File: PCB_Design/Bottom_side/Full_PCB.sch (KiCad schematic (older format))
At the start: 0 parts

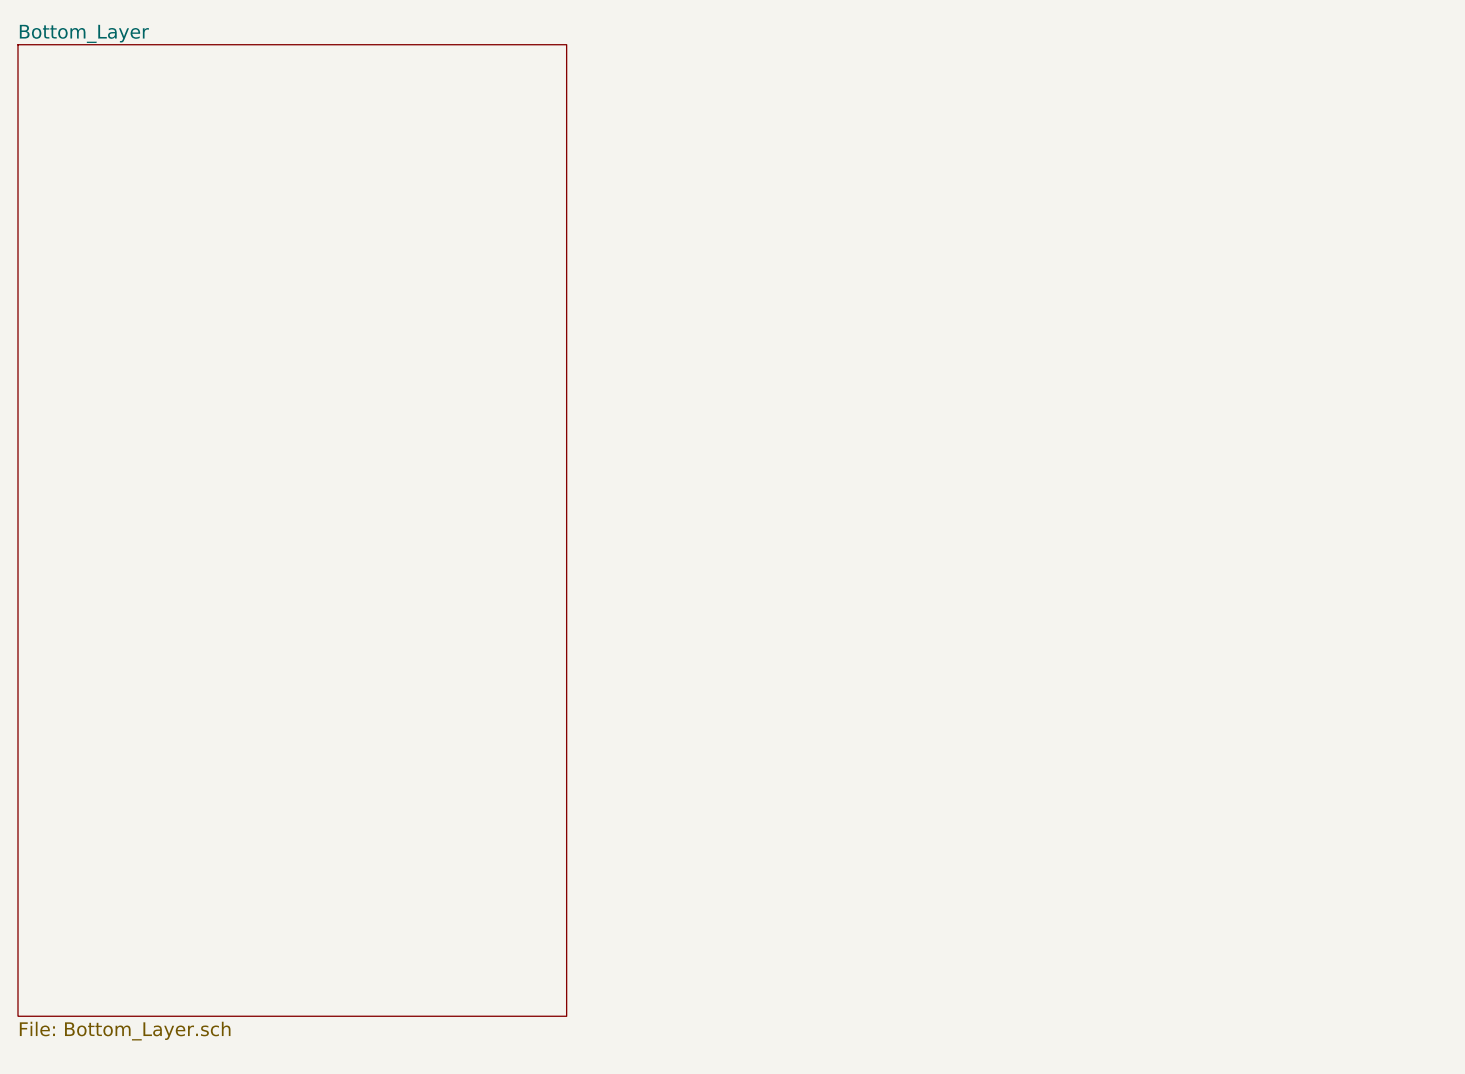
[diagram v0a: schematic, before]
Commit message: Updated PCB structure tree
Full_PCB now includes bottom and top layer hierarchical sheets
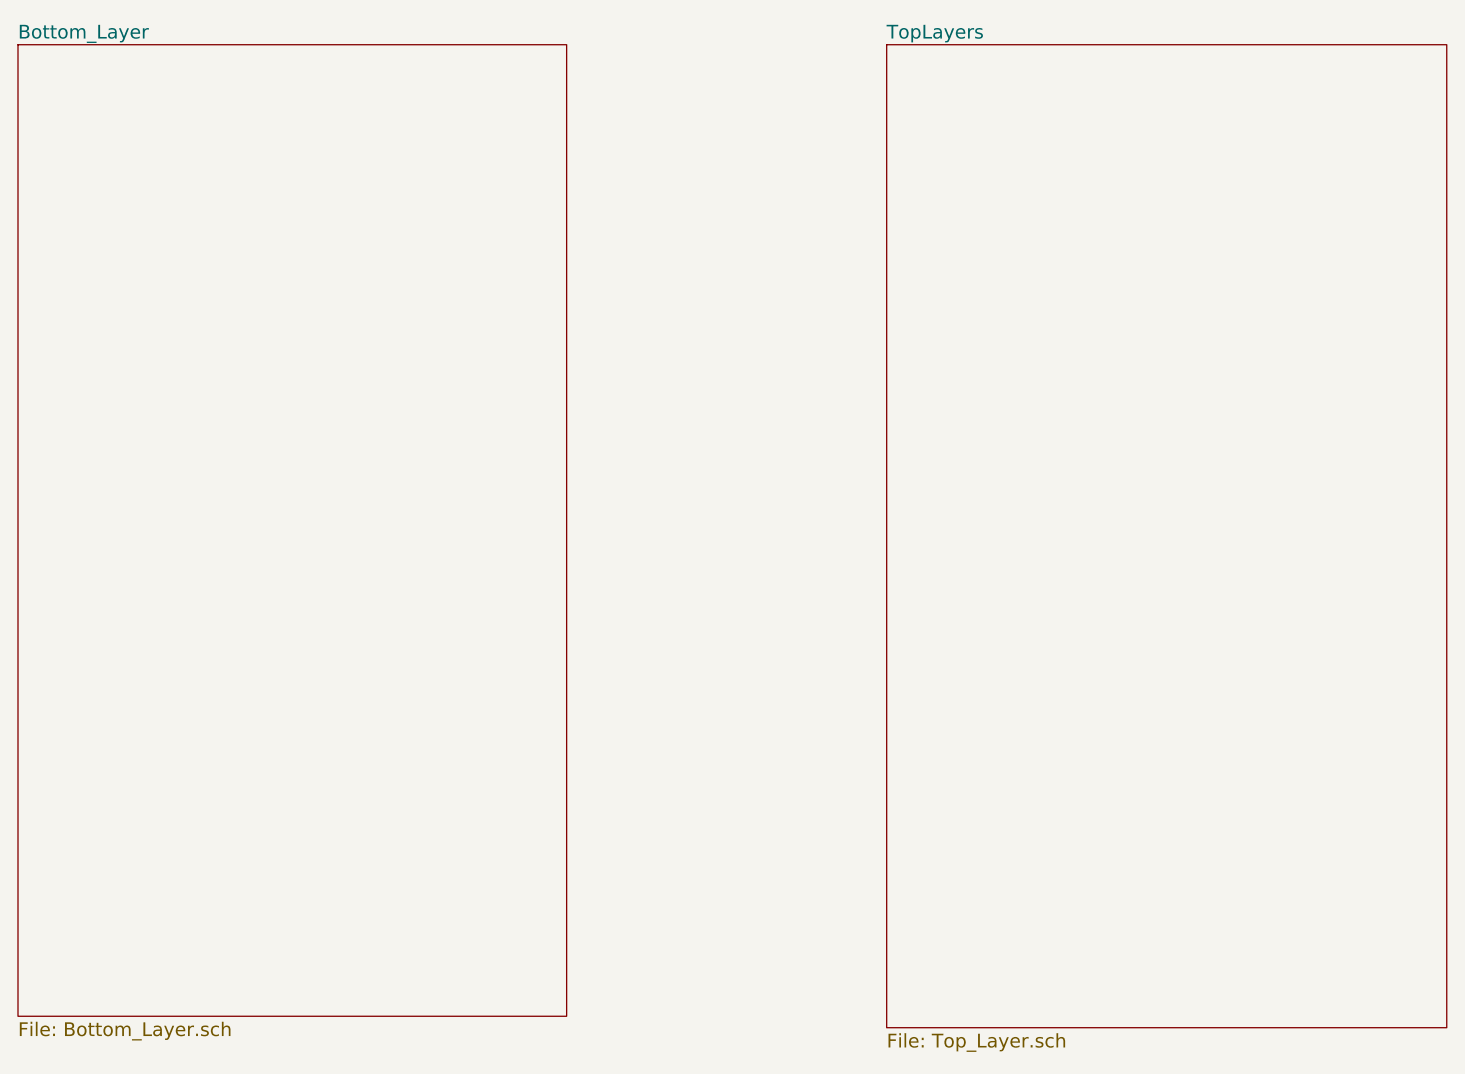
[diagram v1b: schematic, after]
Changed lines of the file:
@@
 $Descr A4 11693 8268
 encoding utf-8
-Sheet 1 3
+Sheet 1 26
 Title ""
 Date ""
@@
 F1 "Bottom_Layer.sch" 60
 $EndSheet
+$Sheet
+S 5900 1650 2450 4300
+U 5A77505C
+F0 "TopLayers" 60
+F1 "Top_Layer.sch" 60
+$EndSheet
 $EndSCHEMATC
